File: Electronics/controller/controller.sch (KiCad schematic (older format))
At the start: 26 parts, among them P1 POWER, P2 PANEL_1, P3 PANEL_2, Q1 P55NF, SW1 SW_PUSH, U1 LM7805CT, U2 74HC595, U3 Arduino_Pro_Micro

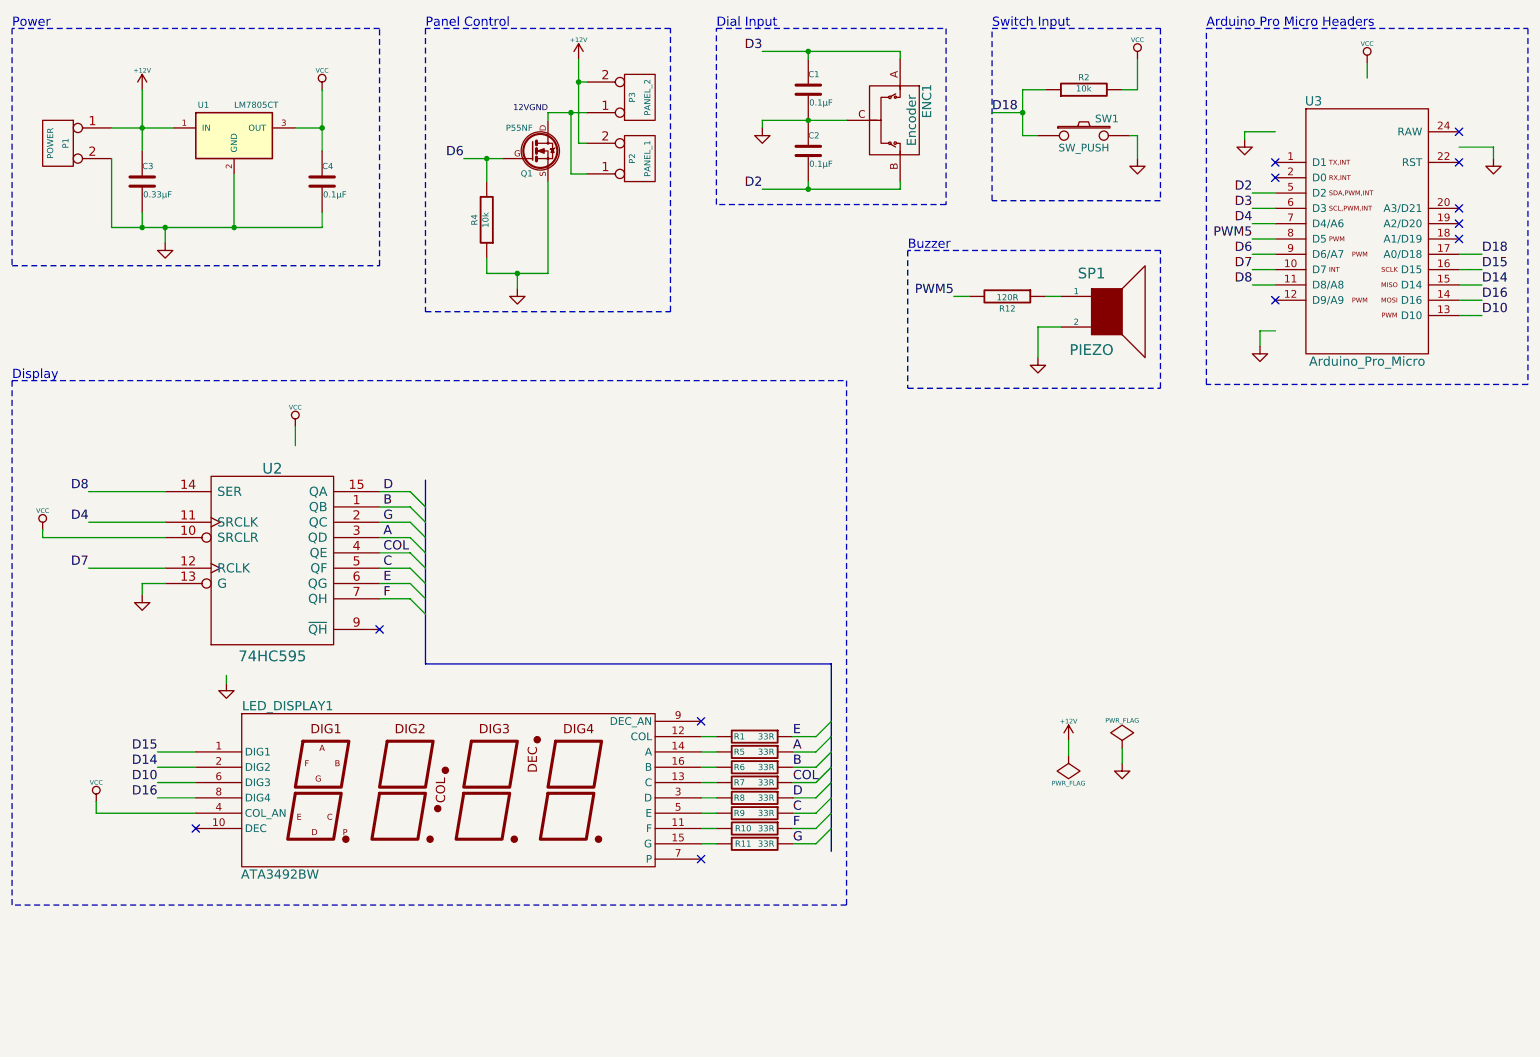
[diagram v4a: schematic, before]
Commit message: Fixes based on first real build.
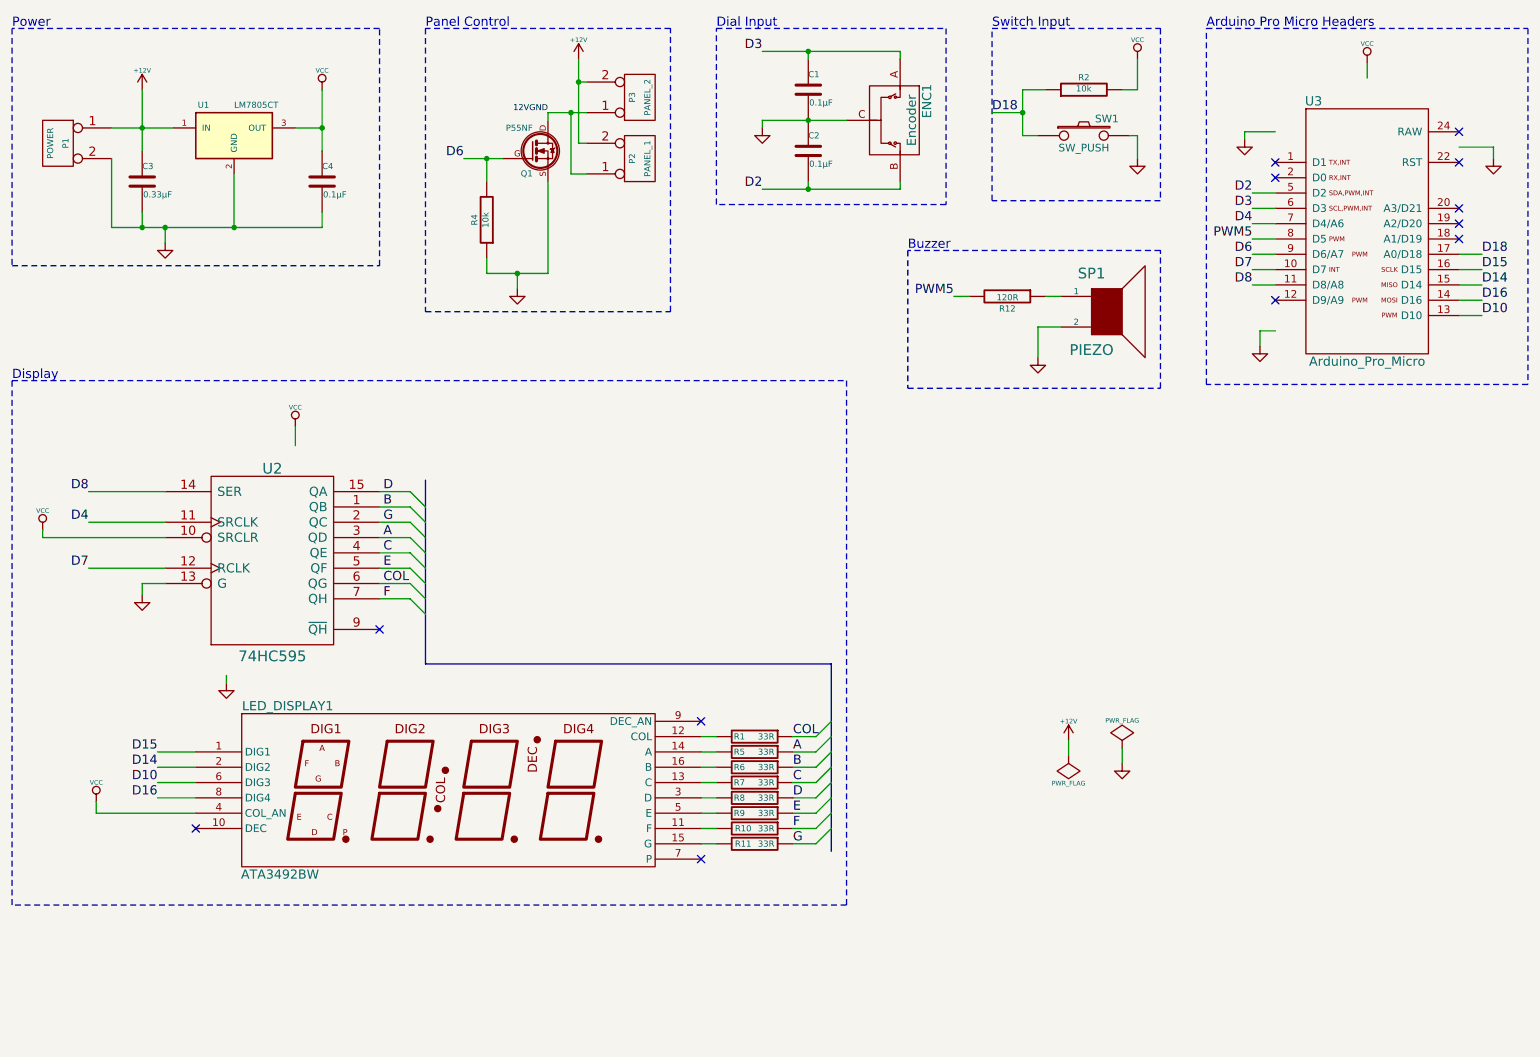
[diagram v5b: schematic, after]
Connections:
- net C: now also R7.1, U2.4 (QE); no longer R9.1, U2.5 (QF)
- net COL: now also R1.1, U2.6 (QG); no longer R7.1, U2.4 (QE)
- net E: now also R9.1, U2.5 (QF); no longer R1.1, U2.6 (QG)
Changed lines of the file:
@@
 D7
 $Comp
-L VCC #PWR09
+L VCC #PWR08
 U 1 1 54886467
 P 1000 4025
-F 0 "#PWR09" H 1000 4115 20  0001 C CNN
+F 0 "#PWR08" H 1000 4115 20  0001 C CNN
 F 1 "VCC" H 1000 4150 30  0000 C CNN
 F 2 "" H 1000 4025 60  0000 C CNN
@@
 B
 Text Label 3225 4275 0    60   ~ 0
-C
+E
 Text Label 3225 4375 0    60   ~ 0
-E
+COL
 Text Label 3225 4475 0    60   ~ 0
 F
@@
 NoConn ~ 10250 1425
 $Comp
-L VCC #PWR010
+L VCC #PWR09
 U 1 1 54886474
 P 2825 1150
-F 0 "#PWR010" H 2825 1240 20  0001 C CNN
+F 0 "#PWR09" H 2825 1240 20  0001 C CNN
 F 1 "VCC" H 2825 1275 30  0000 C CNN
 F 2 "" H 2825 1150 60  0000 C CNN
@@
 	4100 2350 4100 2450
 Wire Wire Line
-	3900 2350 4100 2350
-Wire Wire Line
-	4100 2350 4300 2350
+	3900 2350 4300 2350
 Wire Wire Line
 	4500 1500 4550 1500
@@
 	4450 1700 4550 1700
 Wire Wire Line
-	4500 950  4500 1100
-Wire Wire Line
-	4500 1100 4500 1500
+	4500 950  4500 1500
 Wire Wire Line
 	4500 1100 4550 1100
@@
 	3900 2250 3900 2350
 Wire Wire Line
-	5700 1800 6000 1800
-Wire Wire Line
-	6000 1800 6600 1800
-Wire Wire Line
-	5700 1350 6000 1350
-Wire Wire Line
-	6000 1350 6250 1350
-Wire Wire Line
-	1450 1400 1650 1400
-Wire Wire Line
-	1650 1400 1850 1400
+	5700 1800 6600 1800
+Wire Wire Line
+	5700 1350 6250 1350
+Wire Wire Line
+	1450 1400 1850 1400
 Connection ~ 1650 1400
 Wire Wire Line
-	1650 1150 1650 1400
-Wire Wire Line
-	1650 1400 1650 1550
+	1650 1150 1650 1550
 Wire Wire Line
 	2250 2050 2250 1700
 Wire Wire Line
-	1450 2050 1650 2050
-Wire Wire Line
-	1650 2050 1800 2050
-Wire Wire Line
-	1800 2050 2250 2050
-Wire Wire Line
-	2250 2050 2825 2050
+	1450 2050 2825 2050
 Connection ~ 1800 2050
 Wire Notes Line
@@
 	10700 3075 8600 3075
 Wire Wire Line
-	5700 900  6000 900
-Wire Wire Line
-	6000 900  6600 900
+	5700 900  6600 900
 Wire Wire Line
 	5700 1350 5700 1400
@@
 	4300 1350 4300 1300
 Wire Wire Line
-	4300 1300 4450 1300
-Wire Wire Line
-	4450 1300 4550 1300
+	4300 1300 4550 1300
 Wire Wire Line
 	3900 1750 3900 1600
 Wire Wire Line
-	3750 1600 3900 1600
-Wire Wire Line
-	3900 1600 4000 1600
+	3750 1600 4000 1600
 Wire Wire Line
 	3200 3775 3400 3775
 Text Label 3225 4175 0    60   ~ 0
-COL
+C
 Wire Notes Line
 	10700 750  10700 3075
@@
 B
 Text Label 5900 5875 0    60   ~ 0
-C
+E
 Text Label 5900 5775 0    60   ~ 0
 D
 Text Label 5900 5375 0    60   ~ 0
-E
+COL
 Text Label 5900 5975 0    60   ~ 0
 F
@@
 G
 Text Label 5900 5675 0    60   ~ 0
-COL
+C
 Wire Wire Line
 	5900 5475 6050 5475
@@
 NoConn ~ 2000 5975
 $Comp
-L VCC #PWR011
+L VCC #PWR010
 U 1 1 54889554
 P 1350 5800
-F 0 "#PWR011" H 1350 5890 20  0001 C CNN
+F 0 "#PWR010" H 1350 5890 20  0001 C CNN
 F 1 "VCC" H 1350 5925 30  0000 C CNN
 F 2 "" H 1350 5800 60  0000 C CNN
@@
 12VGND
 $Comp
-L +12V #PWR012
+L +12V #PWR011
 U 1 1 548EE45A
 P 7700 5400
-F 0 "#PWR012" H 7700 5350 20  0001 C CNN
+F 0 "#PWR011" H 7700 5350 20  0001 C CNN
 F 1 "+12V" H 7700 5525 30  0000 C CNN
 F 2 "" H 7700 5400 60  0000 C CNN
@@
 $EndComp
 $Comp
-L GND #PWR013
+L GND #PWR012
 U 1 1 548EE47C
 P 8050 5550
-F 0 "#PWR013" H 8050 5550 30  0001 C CNN
+F 0 "#PWR012" H 8050 5550 30  0001 C CNN
 F 1 "GND" H 8050 5480 30  0001 C CNN
 F 2 "" H 8050 5550 60  0000 C CNN
@@
 	7500 2700 7500 2900
 $Comp
-L GND #PWR014
+L GND #PWR013
 U 1 1 548F1D53
 P 7500 2900
-F 0 "#PWR014" H 7500 2900 30  0001 C CNN
+F 0 "#PWR013" H 7500 2900 30  0001 C CNN
 F 1 "GND" H 7500 2830 30  0001 C CNN
 F 2 "" H 7500 2900 60  0000 C CNN
@@
 	3400 4475 3500 4575
 Wire Bus Line
-	3500 3700 3500 3875
-Wire Bus Line
-	3500 3875 3500 3975
-Wire Bus Line
-	3500 3975 3500 4075
-Wire Bus Line
-	3500 4075 3500 4175
-Wire Bus Line
-	3500 4175 3500 4275
-Wire Bus Line
-	3500 4275 3500 4375
-Wire Bus Line
-	3500 4375 3500 4475
-Wire Bus Line
-	3500 4475 3500 4575
-Wire Bus Line
-	3500 4575 3500 4900
+	3500 3700 3500 4900
 Entry Wire Line
 	6050 5375 6150 5275
@@
 	6050 6075 6150 5975
 Wire Bus Line
-	6150 4900 6150 5275
-Wire Bus Line
-	6150 5275 6150 5375
-Wire Bus Line
-	6150 5375 6150 5475
-Wire Bus Line
-	6150 5475 6150 5575
-Wire Bus Line
-	6150 5575 6150 5675
-Wire Bus Line
-	6150 5675 6150 5775
-Wire Bus Line
-	6150 5775 6150 5875
-Wire Bus Line
-	6150 5875 6150 5975
-Wire Bus Line
-	6150 5975 6150 6125
+	6150 4900 6150 6125
 Wire Wire Line
 	9050 2325 8900 2325
@@
 $EndComp
 Wire Wire Line
-	2825 1150 2825 1400
-Wire Wire Line
-	2825 1400 2825 1550
+	2825 1150 2825 1550
 Connection ~ 2825 1400
 Wire Wire Line
@@
 	8150 1150 8150 950
 $Comp
-L VCC #PWR015
+L VCC #PWR014
 U 1 1 5490EB8A
 P 8150 950
-F 0 "#PWR015" H 8150 1040 20  0001 C CNN
+F 0 "#PWR014" H 8150 1040 20  0001 C CNN
 F 1 "VCC" H 8150 1075 30  0000 C CNN
 F 2 "" H 8150 950 60  0000 C CNN
@@
 $EndComp
 Wire Wire Line
-	7400 1150 7400 1300
-Wire Wire Line
-	7400 1300 7400 1450
+	7400 1150 7400 1450
 Wire Wire Line
 	7400 1450 7500 1450
@@
 	8150 1450 8150 1600
 $Comp
-L GND #PWR016
+L GND #PWR015
 U 1 1 5488646A
 P 8150 1600
-F 0 "#PWR016" H 8150 1600 30  0001 C CNN
+F 0 "#PWR015" H 8150 1600 30  0001 C CNN
 F 1 "GND" H 8150 1530 30  0001 C CNN
 F 2 "" H 8150 1600 60  0000 C CNN
@@
 	2650 3475 2650 3350
 $Comp
-L VCC #PWR017
+L VCC #PWR016
 U 1 1 54943C19
 P 2650 3350
-F 0 "#PWR017" H 2650 3440 20  0001 C CNN
+F 0 "#PWR016" H 2650 3440 20  0001 C CNN
 F 1 "VCC" H 2650 3475 30  0000 C CNN
 F 2 "" H 2650 3350 60  0000 C CNN
@@
 	9650 1075 9650 975
 $Comp
-L VCC #PWR018
+L VCC #PWR017
 U 1 1 5494476E
 P 9650 975
-F 0 "#PWR018" H 9650 1065 20  0001 C CNN
+F 0 "#PWR017" H 9650 1065 20  0001 C CNN
 F 1 "VCC" H 9650 1100 30  0000 C CNN
 F 2 "" H 9650 975 60  0000 C CNN
@@
 $EndComp
 $Comp
-L GND #PWR019
+L GND #PWR018
 U 1 1 549448CB
 P 8950 2825
-F 0 "#PWR019" H 8950 2825 30  0001 C CNN
+F 0 "#PWR018" H 8950 2825 30  0001 C CNN
 F 1 "GND" H 8950 2755 30  0001 C CNN
 F 2 "" H 8950 2825 60  0000 C CNN
@@
 	8850 1425 8850 1475
 $Comp
-L GND #PWR020
+L GND #PWR019
 U 1 1 54944B3E
 P 8850 1475
-F 0 "#PWR020" H 8850 1475 30  0001 C CNN
+F 0 "#PWR019" H 8850 1475 30  0001 C CNN
 F 1 "GND" H 8850 1405 30  0001 C CNN
 F 2 "" H 8850 1475 60  0000 C CNN
@@
 	10475 1525 10475 1600
 $Comp
-L GND #PWR021
+L GND #PWR020
 U 1 1 549458C0
 P 10475 1600
-F 0 "#PWR021" H 10475 1600 30  0001 C CNN
+F 0 "#PWR020" H 10475 1600 30  0001 C CNN
 F 1 "GND" H 10475 1530 30  0001 C CNN
 F 2 "" H 10475 1600 60  0000 C CNN
@@
 $EndComp
 $Comp
-L GND #PWR08
+L GND #PWR021
 U 1 1 54886466
 P 1650 4450
-F 0 "#PWR08" H 1650 4450 30  0001 C CNN
+F 0 "#PWR021" H 1650 4450 30  0001 C CNN
 F 1 "GND" H 1650 4380 30  0001 C CNN
 F 2 "" H 1650 4450 60  0000 C CNN
@@
 $EndComp
 $Comp
-L GND #PWR?
+L GND #PWR022
 U 1 1 549460D9
 P 2200 5025
-F 0 "#PWR?" H 2200 5025 30  0001 C CNN
+F 0 "#PWR022" H 2200 5025 30  0001 C CNN
 F 1 "GND" H 2200 4955 30  0001 C CNN
 F 2 "" H 2200 5025 60  0000 C CNN

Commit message: Some board layout.
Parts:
- removed U3: Arduino_Pro_Micro, Cylindric:ArduinoProMicro, symbol Arduino_Pro_Micro
- added C5, C6: 22pF, Capacitors_ThroughHole:Capacitor4x3RM2.5, symbol C
- added IC1: ATMEGA328P-P, Sockets_DIP:DIP-28__600, symbol ATMEGA328P-P
- added P4: PROG, Pin_Headers:Pin_Header_Angled_1x02, symbol CONN_2
- added R3: 10k, Discret:R3, symbol R
- added SW2: SW_PUSH, Discret:SW_PUSH-12mm, symbol SW_PUSH
- added X1: 16MHz, Crystals:Crystal_HC50-U_Vertical, symbol CRYSTAL
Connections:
- net labels added: A0, A1, A2, A3, A4, A5, D11, D12, D13, D5, PWM9, RX, TX
- net labels removed: D14, D15, D16, PWM5
- wire segments 103 -> 131
- no-connect marks 12 -> 11
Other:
- note removed: "Arduino Pro Micro Headers"

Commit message: Layout updated.
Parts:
- SW2: value SW_PUSH -> RESET; footprint Discret:SW_PUSH-12mm -> Discret:SW_PUSH_SMALL
- renumbered R6 to R5, R5 to R6
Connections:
- net labels removed: D18
- wire segments 131 -> 152
- no-connect marks 11 -> 10
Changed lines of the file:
@@
 $EndComp
 Text Label 7200 1300 0    60   ~ 0
-D18
+D8
 Text Notes 7200 750  0    60   ~ 0
 Switch Input
@@
 $EndComp
 Text Label 3225 3875 0    60   ~ 0
+D
+Text Label 3225 4275 0    60   ~ 0
+C
+Text Label 3225 4375 0    60   ~ 0
+COL
+Text Label 3225 4475 0    60   ~ 0
+F
+Text Label 3225 3775 0    60   ~ 0
+E
+Text Label 3225 3975 0    60   ~ 0
 B
-Text Label 3225 4275 0    60   ~ 0
-COL
-Text Label 3225 4375 0    60   ~ 0
-F
-Text Label 3225 4475 0    60   ~ 0
-E
-Text Label 3225 3775 0    60   ~ 0
-D
-Text Label 3225 3975 0    60   ~ 0
+Text Label 3225 4075 0    60   ~ 0
 G
-Text Label 3225 4075 0    60   ~ 0
-A
 $Comp
 L R R8
@@
 NoConn ~ 3200 4675
 $Comp
-L R R6
+L R R5
 U 1 1 5488646C
 P 5650 5575
-F 0 "R6" V 5650 5475 40  0000 C CNN
+F 0 "R5" V 5650 5475 40  0000 C CNN
 F 1 "33R" V 5650 5650 40  0000 C CNN
 F 2 "Discret:R3" V 5580 5575 30  0001 C CNN
@@
 $EndComp
 $Comp
-L R R5
+L R R6
 U 1 1 54886470
 P 5650 5475
-F 0 "R5" V 5650 5375 40  0000 C CNN
+F 0 "R6" V 5650 5375 40  0000 C CNN
 F 1 "33R" V 5650 5550 40  0000 C CNN
 F 2 "Discret:R3" V 5580 5475 30  0001 C CNN
@@
 $EndComp
 Text Label 3225 4175 0    60   ~ 0
-C
+A
 $Comp
 L ATA3492BW LED_DISPLAY1
@@
 F 0 "IC1" H 6900 6100 40  0000 L BNN
 F 1 "ATMEGA328P-P" H 8050 3450 40  0000 L BNN
-F 2 "Sockets_DIP:DIP-28__600" H 7650 4850 30  0000 C CIN
+F 2 "Sockets_DIP:DIP-28__600" H 7650 4850 30  0001 C CIN
 F 3 "" H 7650 4850 60  0000 C CNN
 	1    7650 4850
@@
 P 9875 5200
 F 0 "SW2" H 10025 5310 50  0000 C CNN
-F 1 "SW_PUSH" H 9875 5120 50  0000 C CNN
-F 2 "Discret:SW_PUSH-12mm" H 9875 5200 60  0001 C CNN
+F 1 "RESET" H 9875 5120 50  0000 C CNN
+F 2 "Discret:SW_PUSH_SMALL" H 9875 5200 60  0001 C CNN
 F 3 "" H 9875 5200 60  0000 C CNN
 	1    9875 5200
@@
 	4100 2350 4100 2450
 Wire Wire Line
-	3900 2350 4300 2350
+	3900 2350 4100 2350
+Wire Wire Line
+	4100 2350 4300 2350
 Wire Wire Line
 	4500 1500 4550 1500
@@
 	4450 1700 4550 1700
 Wire Wire Line
-	4500 950  4500 1500
+	4500 950  4500 1100
+Wire Wire Line
+	4500 1100 4500 1500
 Wire Wire Line
 	4500 1100 4550 1100
@@
 	3900 2250 3900 2350
 Wire Wire Line
-	5700 1800 6600 1800
-Wire Wire Line
-	5700 1350 6250 1350
-Wire Wire Line
-	1450 1400 1850 1400
+	5700 1800 6000 1800
+Wire Wire Line
+	6000 1800 6600 1800
+Wire Wire Line
+	5700 1350 6000 1350
+Wire Wire Line
+	6000 1350 6250 1350
+Wire Wire Line
+	1450 1400 1650 1400
+Wire Wire Line
+	1650 1400 1850 1400
 Connection ~ 1650 1400
 Wire Wire Line
-	1650 1150 1650 1550
+	1650 1150 1650 1400
+Wire Wire Line
+	1650 1400 1650 1550
 Wire Wire Line
 	2250 2050 2250 1700
 Wire Wire Line
-	1450 2050 2825 2050
+	1450 2050 1650 2050
+Wire Wire Line
+	1650 2050 1800 2050
+Wire Wire Line
+	1800 2050 2250 2050
+Wire Wire Line
+	2250 2050 2825 2050
 Connection ~ 1800 2050
 Wire Notes Line
@@
 	5400 1900 5400 750
 Wire Wire Line
-	5700 900  6600 900
+	5700 900  6000 900
+Wire Wire Line
+	6000 900  6600 900
 Wire Wire Line
 	5700 1350 5700 1400
@@
 	4300 1350 4300 1300
 Wire Wire Line
-	4300 1300 4550 1300
+	4300 1300 4450 1300
+Wire Wire Line
+	4450 1300 4550 1300
 Wire Wire Line
 	3900 1750 3900 1600
 Wire Wire Line
-	3750 1600 4000 1600
+	3750 1600 3900 1600
+Wire Wire Line
+	3900 1600 4000 1600
 Wire Wire Line
 	3200 3775 3400 3775
@@
 	3500 4900 6150 4900
 Wire Bus Line
-	3500 3700 3500 4900
-Wire Bus Line
-	6150 4900 6150 6125
+	3500 3700 3500 3875
+Wire Bus Line
+	3500 3875 3500 3975
+Wire Bus Line
+	3500 3975 3500 4075
+Wire Bus Line
+	3500 4075 3500 4175
+Wire Bus Line
+	3500 4175 3500 4275
+Wire Bus Line
+	3500 4275 3500 4375
+Wire Bus Line
+	3500 4375 3500 4475
+Wire Bus Line
+	3500 4475 3500 4575
+Wire Bus Line
+	3500 4575 3500 4900
+Wire Bus Line
+	6150 4900 6150 5275
+Wire Bus Line
+	6150 5275 6150 5375
+Wire Bus Line
+	6150 5375 6150 5475
+Wire Bus Line
+	6150 5475 6150 5575
+Wire Bus Line
+	6150 5575 6150 5675
+Wire Bus Line
+	6150 5675 6150 5775
+Wire Bus Line
+	6150 5775 6150 5875
+Wire Bus Line
+	6150 5875 6150 5975
+Wire Bus Line
+	6150 5975 6150 6125
 Wire Wire Line
 	1800 2050 1800 2150
@@
 Connection ~ 1650 2050
 Wire Wire Line
-	2825 1150 2825 1550
+	2825 1150 2825 1400
+Wire Wire Line
+	2825 1400 2825 1550
 Connection ~ 2825 1400
 Wire Wire Line
@@
 	8150 1150 8150 950
 Wire Wire Line
-	7400 1150 7400 1450
+	7400 1150 7400 1300
+Wire Wire Line
+	7400 1300 7400 1450
 Wire Wire Line
 	7400 1450 7500 1450
@@
 	6750 3750 6650 3750
 Wire Wire Line
-	6650 3650 6650 4350
+	6650 3650 6650 3750
+Wire Wire Line
+	6650 3750 6650 4050
+Wire Wire Line
+	6650 4050 6650 4350
 Wire Wire Line
 	6750 6050 6650 6050
 Wire Wire Line
-	6650 5950 6650 6150
+	6650 5950 6650 6050
+Wire Wire Line
+	6650 6050 6650 6150
 Wire Wire Line
 	6750 5950 6650 5950
@@
 	8650 5200 8925 5200
 Wire Wire Line
-	9425 5200 9575 5200
+	9425 5200 9500 5200
+Wire Wire Line
+	9500 5200 9575 5200
 Wire Wire Line
 	9500 5200 9500 5100
@@
 	9225 4350 9225 4025
 Wire Wire Line
-	9225 4025 10000 4025
+	9225 4025 9500 4025
+Wire Wire Line
+	9500 4025 10000 4025
 Wire Wire Line
 	9500 4025 9500 4075
@@
 	9500 4675 9500 4750
 Wire Wire Line
-	9225 4750 9550 4750
+	9225 4750 9500 4750
+Wire Wire Line
+	9500 4750 9550 4750
 Wire Wire Line
 	9225 4750 9225 4450
@@
 Connection ~ 9500 4025
 Wire Wire Line
-	10000 4500 10000 4850
+	10000 4500 10000 4750
+Wire Wire Line
+	10000 4750 10000 4850
 Connection ~ 9500 4750
 Wire Wire Line
@@
 	9200 5500 9400 5500
 Wire Wire Line
-	8650 5450 9150 5450
-Wire Wire Line
-	9150 5450 9150 5700
-Wire Wire Line
-	9150 5700 9400 5700
+	8650 5450 9100 5450
+Wire Wire Line
+	9100 5450 9100 5700
+Wire Wire Line
+	9100 5700 9400 5700
 Wire Wire Line
 	8650 5550 8850 5550
@@
 NoConn ~ 8850 5000
 NoConn ~ 8850 5100
-NoConn ~ 8850 3750
 $EndSCHEMATC
